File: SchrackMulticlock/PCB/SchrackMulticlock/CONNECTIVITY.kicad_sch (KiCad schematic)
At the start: 26 parts, among them J1 TYPE-C-31-M-12 (USB C CONN), U7 USBLC6-2SC6

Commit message: Multiclock PCB update
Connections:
- net VBATT renamed VBATT_OUT
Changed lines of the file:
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@@
 		)
 	)
-	(global_label "VBATT"
+	(global_label "VBATT_OUT"
 		(shape input)
 		(at 157.48 135.89 180)
@@
 		)
 		(property "Intersheetrefs" "${INTERSHEET_REFS}"
-			(at 151.264 135.89 0)
+			(at 148.1865 135.89 0)
 			(effects
 				(font

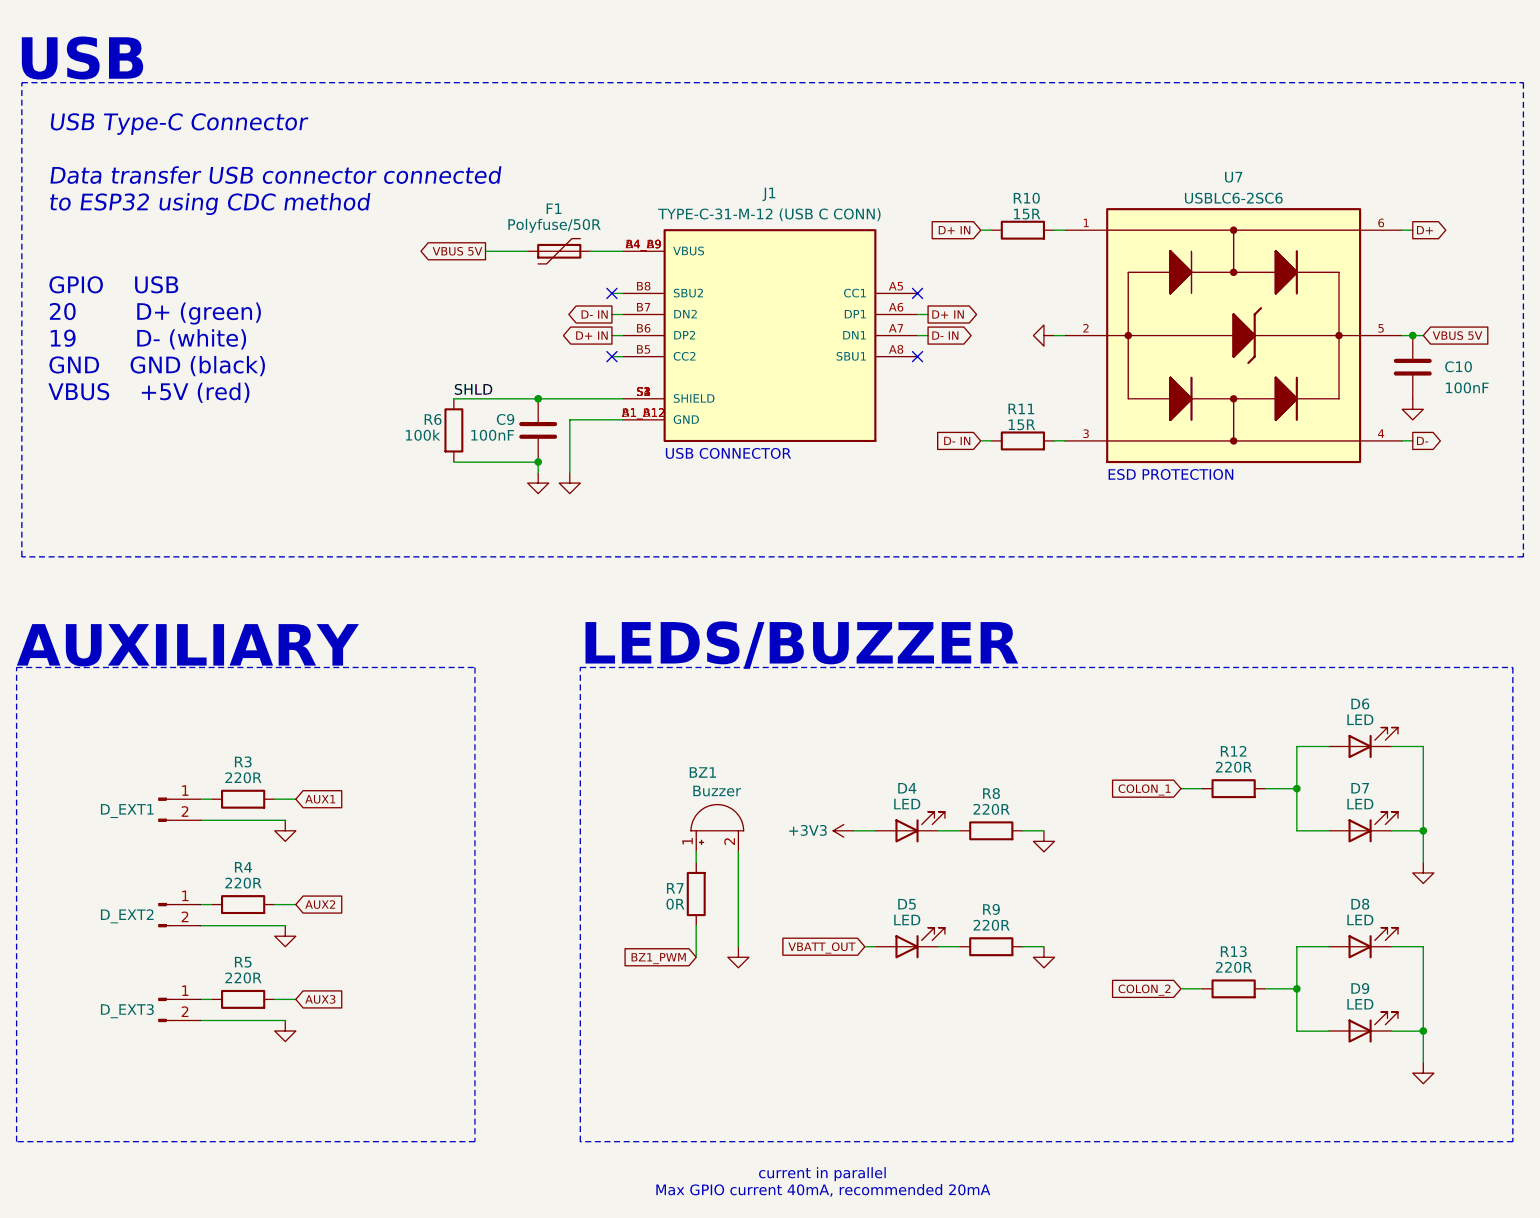
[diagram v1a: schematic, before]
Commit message: SchrackMulticlock PCB final routing
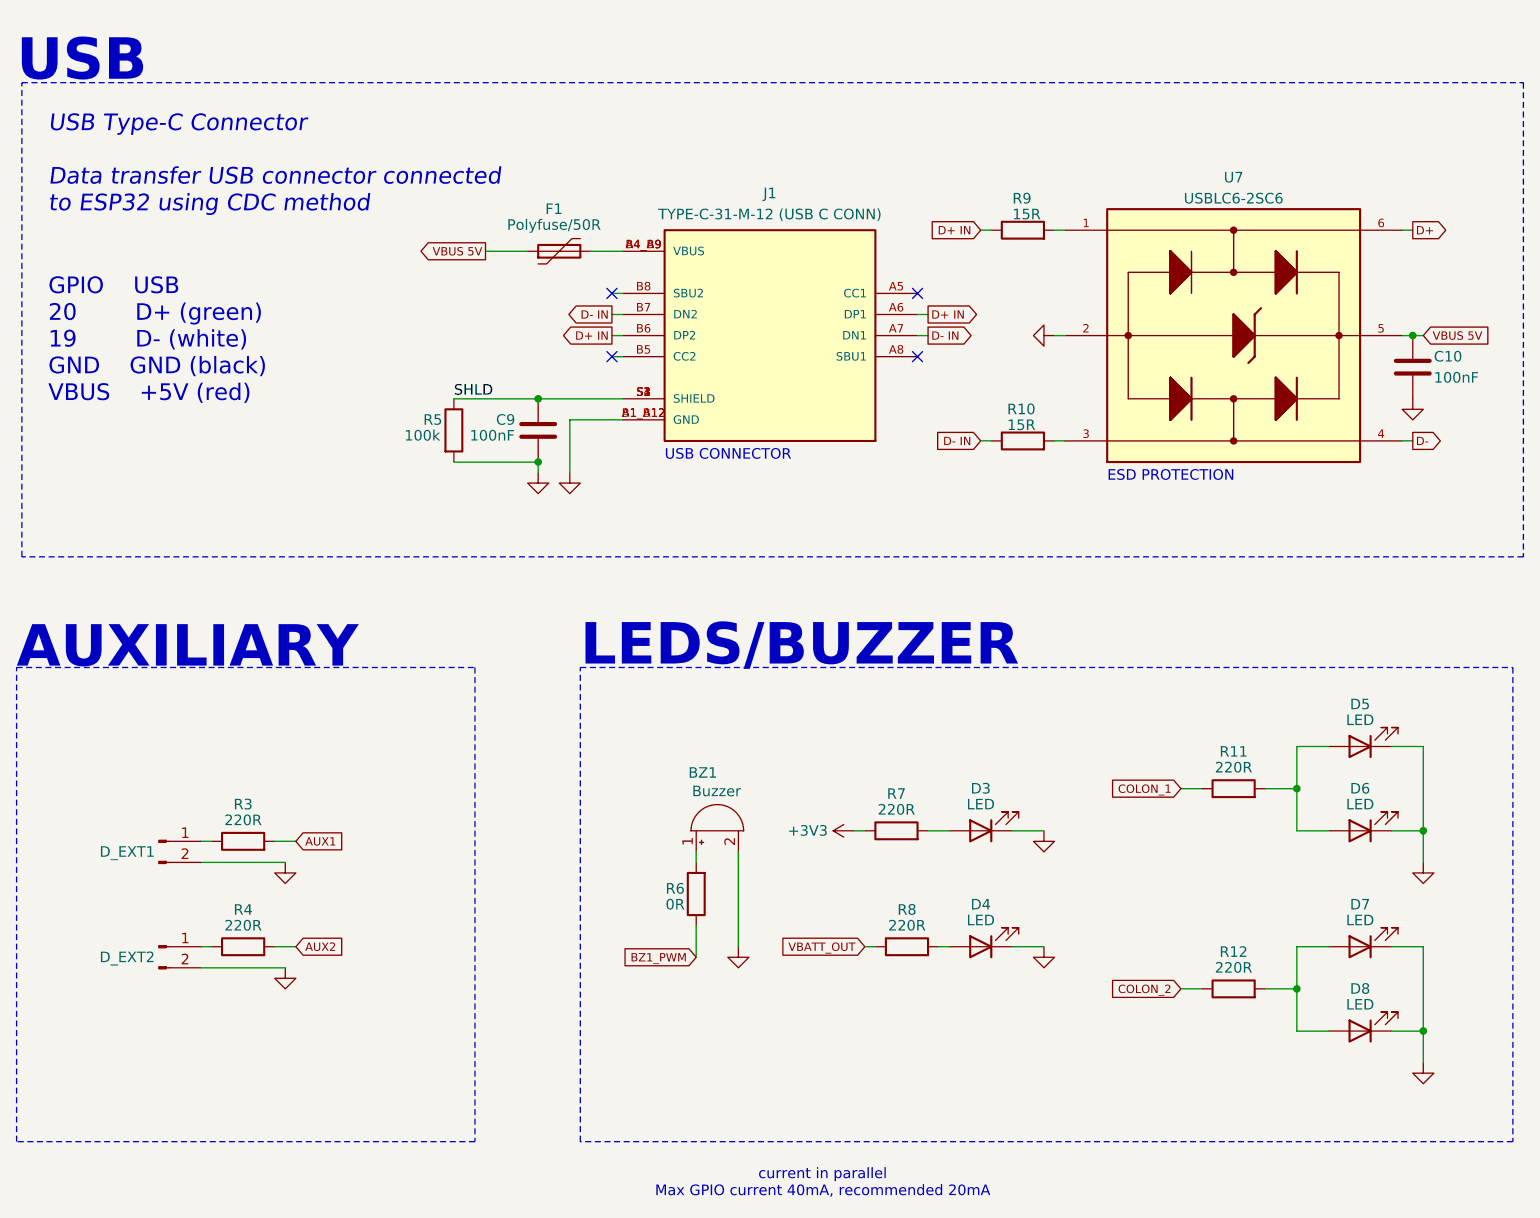
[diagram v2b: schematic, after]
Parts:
- removed D_EXT3: Conn_01x02_Pin, Connector_JST:JST_XH_B2B-XH-A_1x02_P2.50mm_Vertical, symbol Connector:Conn_01x02_Pin
- removed R5, R9: 220R, Resistor_SMD:R_0805_2012Metric_Pad1.20x1.40mm_HandSolder, symbol Device:R
- added R7: 220R, Resistor_SMD:R_0805_2012Metric_Pad1.20x1.40mm_HandSolder, symbol Device:R
- renumbered D4 to D3, D5 to D4, D6 to D5, D7 to D6, D8 to D7, D9 to D8, R11 to R10, R12 to R11, R13 to R12, R6 to R5, R7 to R6, R10 to R9
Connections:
- net +3V3: now also R7.1; no longer D3.2 (A)
- net GND: now also D3.1 (K), D4.1 (K); no longer R8.2
- net VBATT_OUT: now also R8.1; no longer D4.2 (A)
- new net: D4.2 (A), R8.2
- new net: D3.2 (A), R7.2
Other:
- moved on the sheet: D3, D4, D_EXT1, D_EXT2, R3, R4

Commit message: Multiclock silkscreen updafe
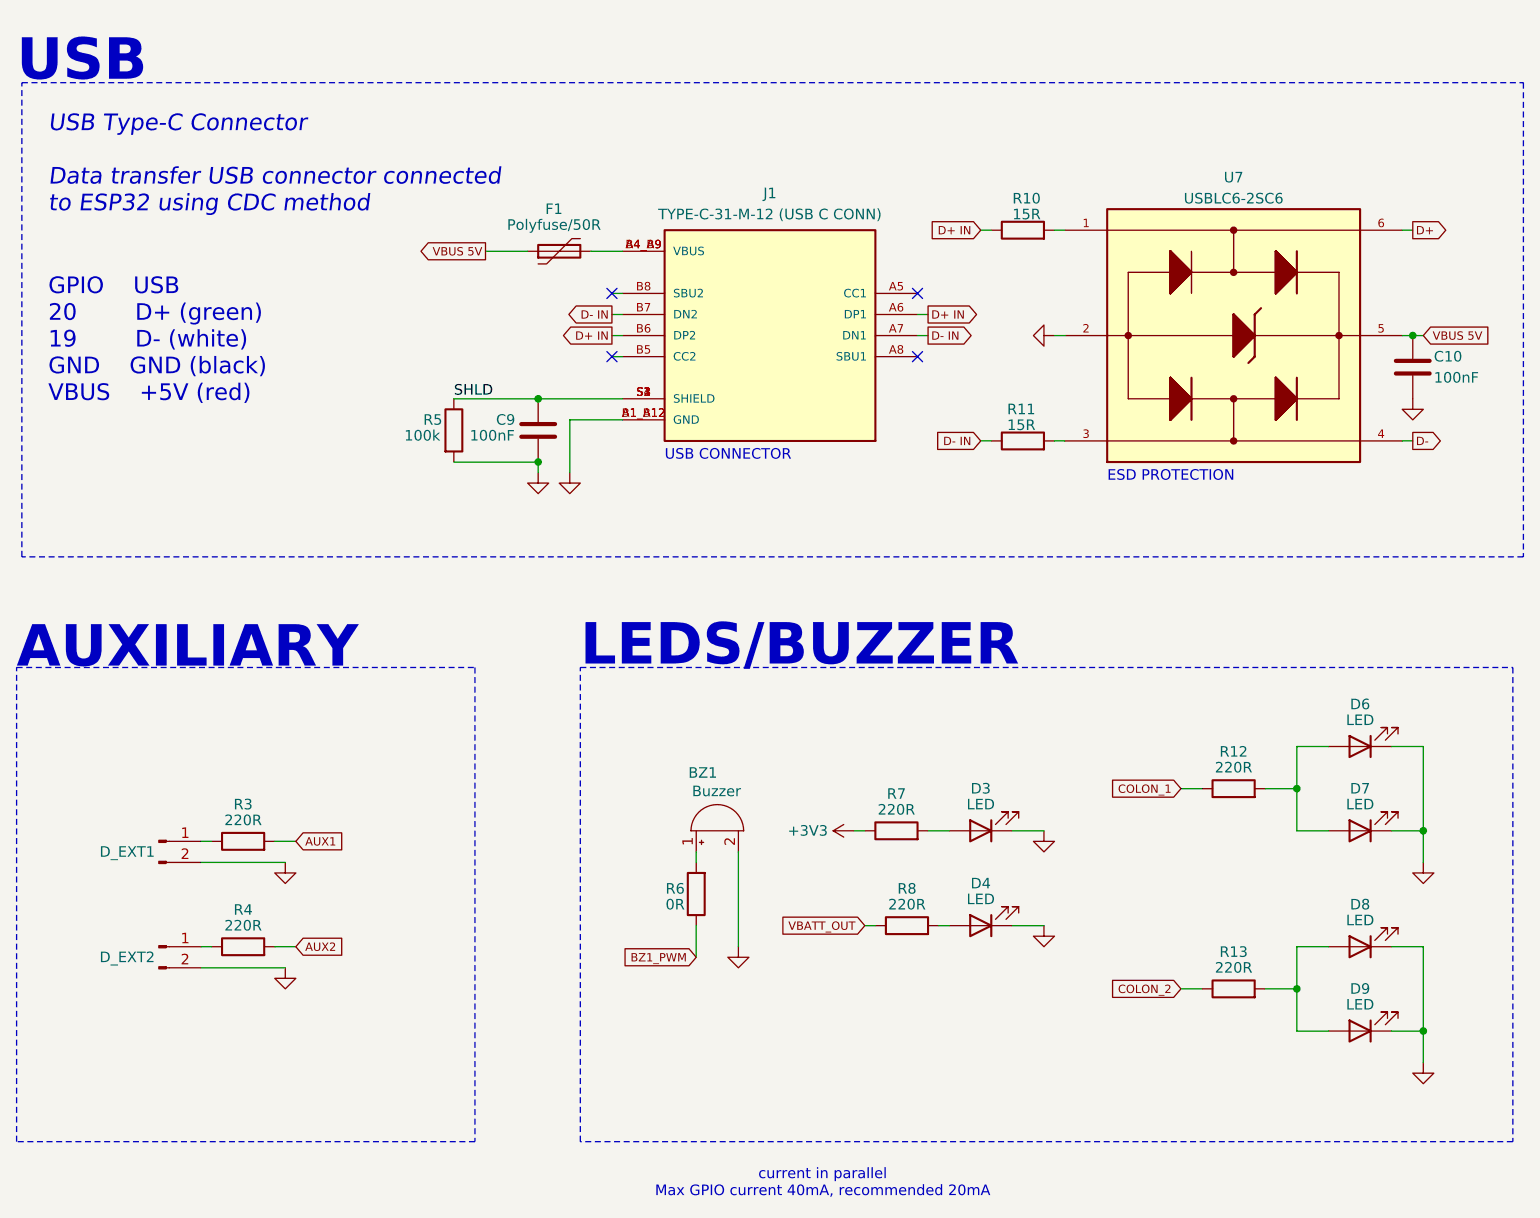
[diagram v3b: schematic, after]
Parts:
- renumbered D5 to D6, D6 to D7, D7 to D8, D8 to D9, R9 to R10, R10 to R11, R11 to R12, R12 to R13
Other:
- moved on the sheet: D4, R8
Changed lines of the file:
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@@
 	(wire
 		(pts
-			(xy 157.48 135.89) (xy 158.75 135.89)
+			(xy 157.48 133.35) (xy 158.75 133.35)
 		)
 		(stroke
@@
 	(wire
 		(pts
-			(xy 167.64 135.89) (xy 166.37 135.89)
+			(xy 167.64 133.35) (xy 166.37 133.35)
 		)
 		(stroke
@@
 	(wire
 		(pts
-			(xy 175.26 135.89) (xy 179.07 135.89)
+			(xy 175.26 133.35) (xy 179.07 133.35)
 		)
 		(stroke
@@
 	(global_label "VBATT_OUT"
 		(shape input)
-		(at 157.48 135.89 180)
+		(at 157.48 133.35 180)
 		(fields_autoplaced yes)
 		(effects
@@
 		)
 		(property "Intersheetrefs" "${INTERSHEET_REFS}"
-			(at 148.1865 135.89 0)
+			(at 148.1865 133.35 0)
 			(effects
 				(font
@@
 	(symbol
 		(lib_id "Device:LED")
-		(at 171.45 135.89 180)
+		(at 171.45 133.35 180)
 		(unit 1)
 		(exclude_from_sim no)
@@
 		(dnp no)
 		(property "Reference" "D4"
-			(at 171.45 130.81 0)
+			(at 171.45 128.27 0)
 			(effects
 				(font
@@
 		)
 		(property "Value" "LED"
-			(at 171.45 132.715 0)
+			(at 171.45 130.175 0)
 			(effects
 				(font
@@
 		)
 		(property "Footprint" "LED_SMD:LED_0805_2012Metric_Pad1.15x1.40mm_HandSolder"
-			(at 171.45 135.89 0)
+			(at 171.45 133.35 0)
 			(effects
 				(font
@@
 		)
 		(property "Datasheet" "~"
-			(at 171.45 135.89 0)
+			(at 171.45 133.35 0)
 			(effects
 				(font
@@
 		)
 		(property "Description" "Light emitting diode"
-			(at 171.45 135.89 0)
+			(at 171.45 133.35 0)
 			(effects
 				(font
@@
 		(on_board yes)
 		(dnp no)
-		(property "Reference" "D6"
+		(property "Reference" "D7"
 			(at 217.17 116.84 0)
 			(effects
@@
 			(project "SchrackMulticlock"
 				(path "/d96f2ffc-3f4c-4f71-b693-29f6b8c3245d/301b3ab9-8372-40d2-93c7-cd7607d23fc4"
-					(reference "D6")
+					(reference "D7")
 					(unit 1)
 				)
@@
 		(dnp no)
 		(fields_autoplaced yes)
-		(property "Reference" "#PWR022"
+		(property "Reference" "#PWR023"
 			(at 173.99 62.23 0)
 			(effects
@@
 			(project "SchrackCounter"
 				(path "/d96f2ffc-3f4c-4f71-b693-29f6b8c3245d/301b3ab9-8372-40d2-93c7-cd7607d23fc4"
-					(reference "#PWR022")
+					(reference "#PWR023")
 					(unit 1)
 				)
@@
 		(on_board yes)
 		(dnp no)
-		(property "Reference" "D7"
+		(property "Reference" "D8"
 			(at 217.17 130.81 0)
 			(effects
@@
 			(project "SchrackMulticlock"
 				(path "/d96f2ffc-3f4c-4f71-b693-29f6b8c3245d/301b3ab9-8372-40d2-93c7-cd7607d23fc4"
-					(reference "D7")
+					(reference "D8")
 					(unit 1)
 				)
@@
 		(dnp no)
 		(fields_autoplaced yes)
-		(property "Reference" "#PWR024"
+		(property "Reference" "#PWR025"
 			(at 224.79 132.08 0)
 			(effects
@@
 			(project "SchrackMulticlock"
 				(path "/d96f2ffc-3f4c-4f71-b693-29f6b8c3245d/301b3ab9-8372-40d2-93c7-cd7607d23fc4"
-					(reference "#PWR024")
+					(reference "#PWR025")
 					(unit 1)
 				)
@@
 	(symbol
 		(lib_id "power:GND")
-		(at 179.07 135.89 0)
+		(at 179.07 133.35 0)
 		(unit 1)
 		(exclude_from_sim no)
@@
 		(fields_autoplaced yes)
 		(property "Reference" "#PWR021"
-			(at 179.07 142.24 0)
+			(at 179.07 139.7 0)
 			(effects
 				(font
@@
 		)
 		(property "Value" "GND"
-			(at 178.435 139.7 90)
+			(at 178.435 137.16 90)
 			(effects
 				(font
@@
 		)
 		(property "Footprint" ""
-			(at 179.07 135.89 0)
+			(at 179.07 133.35 0)
 			(effects
 				(font
@@
 		)
 		(property "Datasheet" ""
-			(at 179.07 135.89 0)
+			(at 179.07 133.35 0)
 			(effects
 				(font
@@
 		)
 		(property "Description" ""
-			(at 179.07 135.89 0)
+			(at 179.07 133.35 0)
 			(effects
 				(font
@@
 		(on_board yes)
 		(dnp no)
-		(property "Reference" "R10"
+		(property "Reference" "R11"
 			(at 174.625 71.12 90)
 			(effects
@@
 			(project "SchrackCounter"
 				(path "/d96f2ffc-3f4c-4f71-b693-29f6b8c3245d/301b3ab9-8372-40d2-93c7-cd7607d23fc4"
-					(reference "R10")
+					(reference "R11")
 					(unit 1)
 				)
@@
 		(dnp no)
 		(fields_autoplaced yes)
-		(property "Reference" "#PWR025"
+		(property "Reference" "#PWR026"
 			(at 224.79 156.21 0)
 			(effects
@@
 			(project "SchrackMulticlock"
 				(path "/d96f2ffc-3f4c-4f71-b693-29f6b8c3245d/301b3ab9-8372-40d2-93c7-cd7607d23fc4"
-					(reference "#PWR025")
+					(reference "#PWR026")
 					(unit 1)
 				)
@@
 		(on_board yes)
 		(dnp no)
-		(property "Reference" "R9"
+		(property "Reference" "R10"
 			(at 175.26 45.72 90)
 			(effects
@@
 			(project "SchrackCounter"
 				(path "/d96f2ffc-3f4c-4f71-b693-29f6b8c3245d/301b3ab9-8372-40d2-93c7-cd7607d23fc4"
-					(reference "R9")
+					(reference "R10")
 					(unit 1)
 				)
@@
 	(symbol
 		(lib_id "Device:R")
-		(at 162.56 135.89 90)
+		(at 162.56 133.35 90)
 		(unit 1)
 		(exclude_from_sim no)
@@
 		(dnp no)
 		(property "Reference" "R8"
-			(at 162.56 131.445 90)
+			(at 162.56 128.905 90)
 			(effects
 				(font
@@
 		)
 		(property "Value" "220R"
-			(at 162.56 133.35 90)
+			(at 162.56 130.81 90)
 			(effects
 				(font
@@
 		)
 		(property "Footprint" "Resistor_SMD:R_0805_2012Metric_Pad1.20x1.40mm_HandSolder"
-			(at 162.56 137.668 90)
+			(at 162.56 135.128 90)
 			(effects
 				(font
@@
 		)
 		(property "Datasheet" "~"
-			(at 162.56 135.89 0)
+			(at 162.56 133.35 0)
 			(effects
 				(font
@@
 		)
 		(property "Description" "Resistor"
-			(at 162.56 135.89 0)
+			(at 162.56 133.35 0)
 			(effects
 				(font
@@
 		(on_board yes)
 		(dnp no)
-		(property "Reference" "R12"
+		(property "Reference" "R13"
 			(at 201.93 136.525 90)
 			(effects
@@
 			(project "SchrackMulticlock"
 				(path "/d96f2ffc-3f4c-4f71-b693-29f6b8c3245d/301b3ab9-8372-40d2-93c7-cd7607d23fc4"
-					(reference "R12")
+					(reference "R13")
 					(unit 1)
 				)
@@
 		(on_board yes)
 		(dnp no)
-		(property "Reference" "D8"
+		(property "Reference" "D9"
 			(at 217.17 140.97 0)
 			(effects
@@
 			(project "SchrackMulticlock"
 				(path "/d96f2ffc-3f4c-4f71-b693-29f6b8c3245d/301b3ab9-8372-40d2-93c7-cd7607d23fc4"
-					(reference "D8")
+					(reference "D9")
 					(unit 1)
 				)
@@
 		(dnp no)
 		(fields_autoplaced yes)
-		(property "Reference" "#PWR023"
+		(property "Reference" "#PWR024"
 			(at 223.52 76.2 0)
 			(effects
@@
 			(project "SchrackCounter"
 				(path "/d96f2ffc-3f4c-4f71-b693-29f6b8c3245d/301b3ab9-8372-40d2-93c7-cd7607d23fc4"
-					(reference "#PWR023")
+					(reference "#PWR024")
 					(unit 1)
 				)
@@
 		(on_board yes)
 		(dnp no)
-		(property "Reference" "R11"
+		(property "Reference" "R12"
 			(at 201.93 112.395 90)
 			(effects
@@
 			(project "SchrackMulticlock"
 				(path "/d96f2ffc-3f4c-4f71-b693-29f6b8c3245d/301b3ab9-8372-40d2-93c7-cd7607d23fc4"
-					(reference "R11")
+					(reference "R12")
 					(unit 1)
 				)
@@
 		(on_board yes)
 		(dnp no)
-		(property "Reference" "D5"
+		(property "Reference" "D6"
 			(at 217.17 106.68 0)
 			(effects
@@
 			(project "SchrackMulticlock"
 				(path "/d96f2ffc-3f4c-4f71-b693-29f6b8c3245d/301b3ab9-8372-40d2-93c7-cd7607d23fc4"
-					(reference "D5")
+					(reference "D6")
 					(unit 1)
 				)

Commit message: PCB order plotting
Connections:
- net VBATT_OUT renamed +5V
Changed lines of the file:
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@@
-		)
-	)
-	(global_label "VBATT_OUT"
-		(shape input)
-		(at 157.48 133.35 180)
-		(fields_autoplaced yes)
-		(effects
-			(font
-				(face "Bahnschrift")
-				(size 1 1)
-				(color 0 0 0 1)
-			)
-			(justify right)
-		)
-		(property "Intersheetrefs" "${INTERSHEET_REFS}"
-			(at 148.1865 133.35 0)
-			(effects
-				(font
-					(size 1.27 1.27)
-				)
-				(justify right)
-				(hide yes)
-			)
 		)
 	)
@@
 					(unit 1)
 				)
+			)
+		)
+	)
+	(symbol
+		(lib_id "power:+5V")
+		(at 157.48 133.35 90)
+		(unit 1)
+		(exclude_from_sim no)
+		(in_bom yes)
+		(on_board yes)
+		(dnp no)
+		(property "Reference" "#PWR022"
+			(at 161.29 133.35 0)
+			(effects
+				(font
+					(size 1.27 1.27)
+				)
+				(hide yes)
+			)
+		)
+		(property "Value" "+5V"
+			(at 154.305 133.35 90)
+			(effects
+				(font
+					(size 1.27 1.27)
+				)
+				(justify left)
+			)
+		)
+		(property "Footprint" ""
+			(at 157.48 133.35 0)
+			(effects
+				(font
+					(size 1.27 1.27)
+				)
+				(hide yes)
+			)
+		)
+		(property "Datasheet" ""
+			(at 157.48 133.35 0)
+			(effects
+				(font
+					(size 1.27 1.27)
+				)
+				(hide yes)
+			)
+		)
+		(property "Description" "Power symbol creates a global label with name \"+5V\""
+			(at 157.48 133.35 0)
+			(effects
+				(font
+					(size 1.27 1.27)
+				)
+				(hide yes)
+			)
+		)
+		(pin "1"
+		)
+		(instances
+			(project "SchrackMulticlock"
+				(path "/d96f2ffc-3f4c-4f71-b693-29f6b8c3245d/301b3ab9-8372-40d2-93c7-cd7607d23fc4"
+					(reference "#PWR022")
+					(unit 1)
+				)
